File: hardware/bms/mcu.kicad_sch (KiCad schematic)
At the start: 53 parts, among them SW2 SW_Push, SW3 SW_Push, U4 LM5166X, U5 TPS62172DSG, U6 ESP32-C3-MINI-1-N4, U7 SN74LXC1T14DCKR

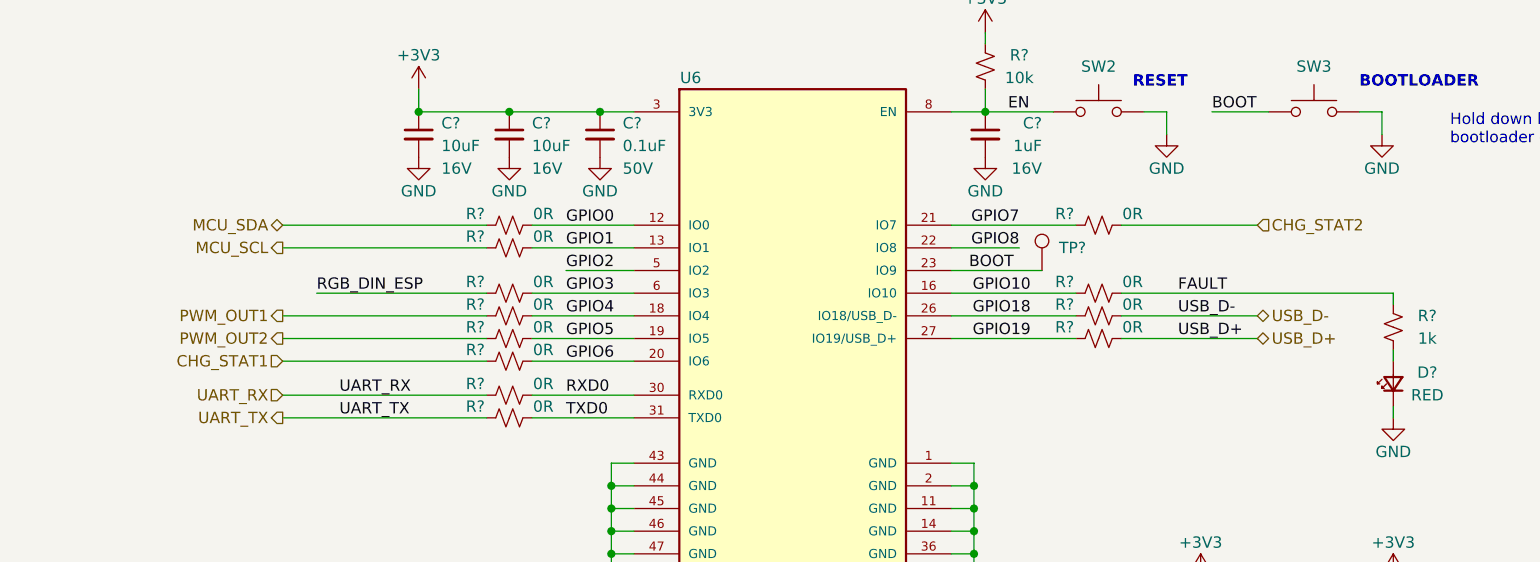
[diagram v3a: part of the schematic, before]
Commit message: Continued layout, defined board area based on mech assembly
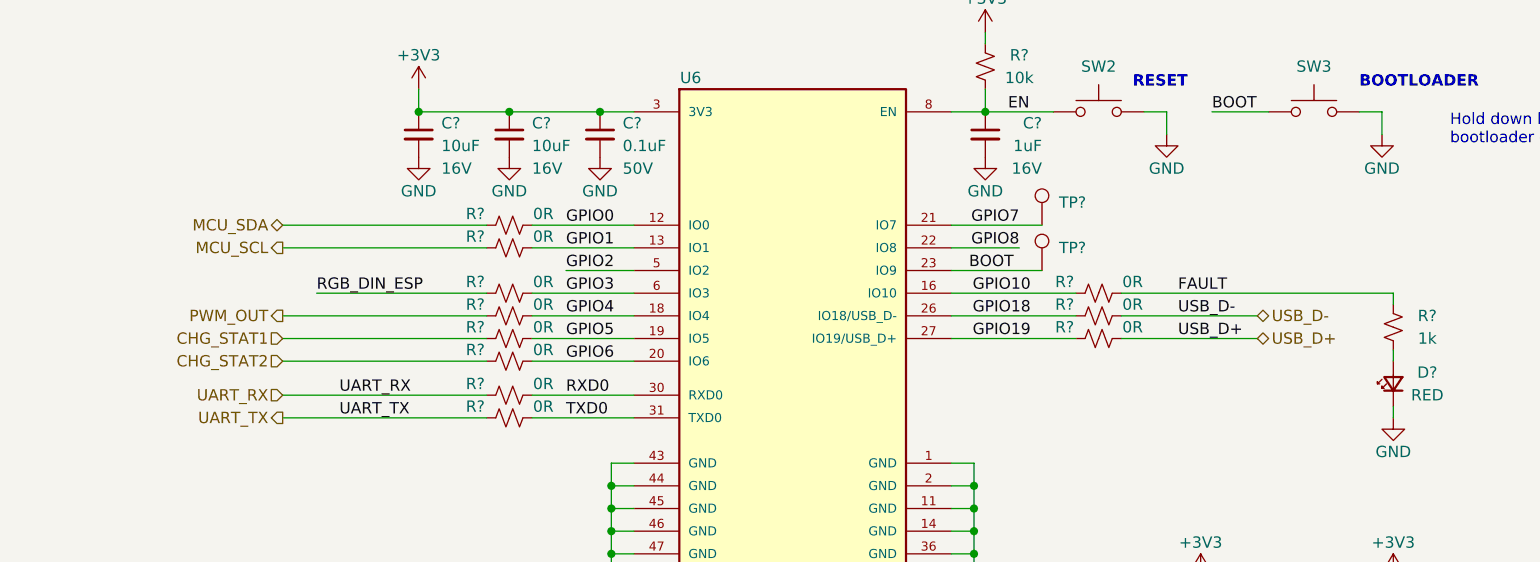
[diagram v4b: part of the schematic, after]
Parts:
- removed R?: 0R, Resistor_SMD:R_0603_1608Metric, symbol Device:R_Small_US
- added TP?: TestPoint, TestPoint:TestPoint_Pad_D1.0mm, symbol Connector:TestPoint
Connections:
- net CHG_STAT1: now also R?.1; no longer R?.1
- net CHG_STAT2: now also R?.1; no longer R?.2
- net GPIO5: now also R?.2
- net GPIO7: now also TP?.1; no longer R?.1
- net PWM_OUT1 renamed PWM_OUT
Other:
- moved on the sheet: R?
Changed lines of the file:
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@@
     (stroke (width 0) (type default))
   )
-  (wire (pts (xy 157.48 97.79) (xy 171.45 97.79))
+  (wire (pts (xy 157.48 97.79) (xy 167.64 97.79))
     (stroke (width 0) (type default))
   )
@@
     (stroke (width 0) (type default))
   )
+  (wire (pts (xy 82.55 110.49) (xy 105.41 110.49))
+    (stroke (width 0) (type default))
+  )
   (wire (pts (xy 160.02 144.78) (xy 160.02 142.24))
     (stroke (width 0) (type default))
@@
     (stroke (width 0) (type default))
   )
-  (wire (pts (xy 82.55 110.49) (xy 105.41 110.49))
-    (stroke (width 0) (type default))
-  )
   (wire (pts (xy 135.89 39.37) (xy 135.89 41.91))
     (stroke (width 0) (type default))
@@
   )
   (wire (pts (xy 91.44 172.72) (xy 99.06 172.72))
-    (stroke (width 0) (type default))
-  )
-  (wire (pts (xy 176.53 97.79) (xy 191.77 97.79))
     (stroke (width 0) (type default))
   )
@@
     (effects (font (size 1.27 1.27)) (justify left))
   )
-  (hierarchical_label "CHG_STAT2" (shape input) (at 191.77 97.79 0) (fields_autoplaced)
-    (effects (font (size 1.27 1.27)) (justify left))
-  )
-  (hierarchical_label "PWM_OUT1" (shape output) (at 82.55 107.95 180) (fields_autoplaced)
+  (hierarchical_label "CHG_STAT2" (shape input) (at 82.55 113.03 180) (fields_autoplaced)
+    (effects (font (size 1.27 1.27)) (justify right))
+  )
+  (hierarchical_label "PWM_OUT" (shape output) (at 82.55 107.95 180) (fields_autoplaced)
     (effects (font (size 1.27 1.27)) (justify right))
   )
@@
     (effects (font (size 1.27 1.27)) (justify right))
   )
-  (hierarchical_label "PWM_OUT2" (shape output) (at 82.55 110.49 180) (fields_autoplaced)
-    (effects (font (size 1.27 1.27)) (justify right))
-  )
-  (hierarchical_label "CHG_STAT1" (shape input) (at 82.55 113.03 180) (fields_autoplaced)
+  (hierarchical_label "CHG_STAT1" (shape input) (at 82.55 110.49 180) (fields_autoplaced)
     (effects (font (size 1.27 1.27)) (justify right))
   )
@@
     )
   )
-  (symbol (lib_id "Device:R_Small_US") (at 173.99 97.79 90) (unit 1)
-    (in_bom yes) (on_board yes) (dnp no)
-    (property "Reference" "R?" (at 170.18 96.52 90)
-      (effects (font (size 1.27 1.27)))
-    )
-    (property "Value" "0R" (at 177.8 96.52 90)
-      (effects (font (size 1.27 1.27)))
-    )
-    (property "Footprint" "Resistor_SMD:R_0603_1608Metric" (at 173.99 97.79 0)
-      (effects (font (size 1.27 1.27)) hide)
-    )
-    (property "Datasheet" "~" (at 173.99 97.79 0)
-      (effects (font (size 1.27 1.27)) hide)
-    )
-    (property "MFG" "Panasonic Electronic Components" (at 173.99 97.79 90)
-      (effects (font (size 1.27 1.27)) hide)
-    )
-    (property "MFG PN" "ERJ-3GEY0R00V" (at 173.99 97.79 90)
+  (symbol (lib_id "Device:R_Small_US") (at 107.95 110.49 90) (unit 1)
+    (in_bom yes) (on_board yes) (dnp no)
+    (property "Reference" "R?" (at 104.14 109.22 90)
+      (effects (font (size 1.27 1.27)))
+    )
+    (property "Value" "0R" (at 111.76 109.22 90)
+      (effects (font (size 1.27 1.27)))
+    )
+    (property "Footprint" "Resistor_SMD:R_0603_1608Metric" (at 107.95 110.49 0)
+      (effects (font (size 1.27 1.27)) hide)
+    )
+    (property "Datasheet" "~" (at 107.95 110.49 0)
+      (effects (font (size 1.27 1.27)) hide)
+    )
+    (property "MFG" "Panasonic Electronic Components" (at 107.95 110.49 90)
+      (effects (font (size 1.27 1.27)) hide)
+    )
+    (property "MFG PN" "ERJ-3GEY0R00V" (at 107.95 110.49 90)
       (effects (font (size 1.27 1.27)) hide)
     )
@@
         (path "/a4805e9d-b940-444e-a7cb-db4f4c53ed46/00000000-0000-0000-0000-00006658c265"
           (reference "#PWR038") (unit 1)
+        )
+      )
+    )
+  )
+  (symbol (lib_id "Connector:TestPoint") (at 167.64 97.79 0) (unit 1)
+    (in_bom yes) (on_board yes) (dnp no)
+    (property "Reference" "TP?" (at 169.545 95.25 0)
+      (effects (font (size 1.27 1.27)) (justify left))
+    )
+    (property "Value" "TestPoint" (at 169.1132 97.1042 0)
+      (effects (font (size 1.27 1.27)) (justify left) hide)
+    )
+    (property "Footprint" "TestPoint:TestPoint_Pad_D1.0mm" (at 172.72 97.79 0)
+      (effects (font (size 1.27 1.27)) hide)
+    )
+    (property "Datasheet" "~" (at 172.72 97.79 0)
+      (effects (font (size 1.27 1.27)) hide)
+    )
+    (pin "1")
+    (instances
+      (project "bms"
+        (path "/a4805e9d-b940-444e-a7cb-db4f4c53ed46/00000000-0000-0000-0000-00006523a805"
+          (reference "TP?") (unit 1)
+        )
+        (path "/a4805e9d-b940-444e-a7cb-db4f4c53ed46/00000000-0000-0000-0000-00006658c265"
+          (reference "TP65") (unit 1)
         )
       )
@@
         )
       )
-    )
-  )
-  (symbol (lib_id "Device:R_Small_US") (at 107.95 110.49 90) (unit 1)
-    (in_bom yes) (on_board yes) (dnp no)
-    (property "Reference" "R?" (at 104.14 109.22 90)
-      (effects (font (size 1.27 1.27)))
-    )
-    (property "Value" "0R" (at 111.76 109.22 90)
-      (effects (font (size 1.27 1.27)))
-    )
-    (property "Footprint" "Resistor_SMD:R_0603_1608Metric" (at 107.95 110.49 0)
-      (effects (font (size 1.27 1.27)) hide)
-    )
-    (property "Datasheet" "~" (at 107.95 110.49 0)
-      (effects (font (size 1.27 1.27)) hide)
-    )
-    (property "MFG" "Panasonic Electronic Components" (at 107.95 110.49 90)
-      (effects (font (size 1.27 1.27)) hide)
-    )
-    (property "MFG PN" "ERJ-3GEY0R00V" (at 107.95 110.49 90)
-      (effects (font (size 1.27 1.27)) hide)
-    )
-    (pin "1")
-    (pin "2")
-    (instances
-      (project "bms"
-        (path "/a4805e9d-b940-444e-a7cb-db4f4c53ed46/00000000-0000-0000-0000-00006523a805"
-          (reference "R?") (unit 1)
-        )
-        (path "/a4805e9d-b940-444e-a7cb-db4f4c53ed46/00000000-0000-0000-0000-00006658c265"
-          (reference "R72") (unit 1)
-        )
-      )

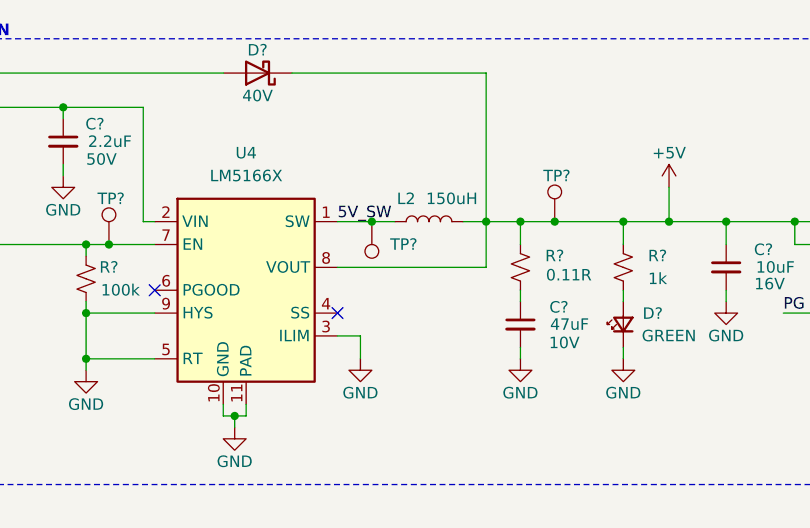
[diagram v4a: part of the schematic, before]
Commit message: Updated test points to 0.5mm to save space, continued layout
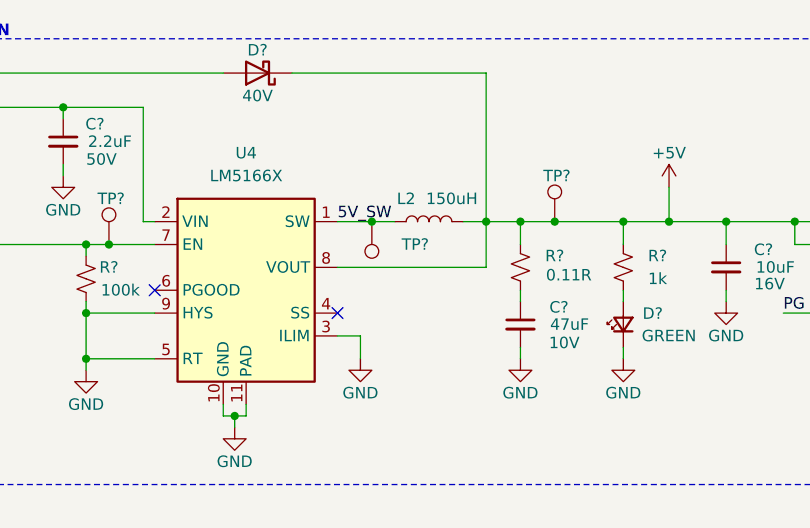
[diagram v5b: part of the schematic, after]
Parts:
- TP? (x9): footprint TestPoint:TestPoint_Pad_D1.0mm -> bms:TestPoint_Pad_D0.5mm; now left out of the parts list
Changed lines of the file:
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@@
   )
   (symbol (lib_id "Connector:TestPoint") (at 99.06 172.72 180) (unit 1)
-    (in_bom yes) (on_board yes) (dnp no)
+    (in_bom no) (on_board yes) (dnp no)
     (property "Reference" "TP?" (at 101.3409 178.1614 0)
       (effects (font (size 1.27 1.27)) (justify left))
@@
       (effects (font (size 1.27 1.27)) (justify left) hide)
     )
-    (property "Footprint" "TestPoint:TestPoint_Pad_D1.0mm" (at 93.98 172.72 0)
+    (property "Footprint" "bms:TestPoint_Pad_D0.5mm" (at 93.98 172.72 0)
       (effects (font (size 1.27 1.27)) hide)
     )
@@
   )
   (symbol (lib_id "Connector:TestPoint") (at 128.27 39.37 0) (unit 1)
-    (in_bom yes) (on_board yes) (dnp no)
+    (in_bom no) (on_board yes) (dnp no)
     (property "Reference" "TP?" (at 127 34.29 0)
       (effects (font (size 1.27 1.27)) (justify left))
@@
       (effects (font (size 1.27 1.27)) (justify left) hide)
     )
-    (property "Footprint" "TestPoint:TestPoint_Pad_D1.0mm" (at 133.35 39.37 0)
+    (property "Footprint" "bms:TestPoint_Pad_D0.5mm" (at 133.35 39.37 0)
       (effects (font (size 1.27 1.27)) hide)
     )
@@
   )
   (symbol (lib_id "Connector:TestPoint") (at 73.66 172.72 180) (unit 1)
-    (in_bom yes) (on_board yes) (dnp no)
+    (in_bom no) (on_board yes) (dnp no)
     (property "Reference" "TP?" (at 75.7005 178.1614 0)
       (effects (font (size 1.27 1.27)) (justify left))
@@
       (effects (font (size 1.27 1.27)) (justify left) hide)
     )
-    (property "Footprint" "TestPoint:TestPoint_Pad_D1.0mm" (at 68.58 172.72 0)
+    (property "Footprint" "bms:TestPoint_Pad_D0.5mm" (at 68.58 172.72 0)
       (effects (font (size 1.27 1.27)) hide)
     )
@@
   )
   (symbol (lib_id "Connector:TestPoint") (at 167.64 97.79 0) (unit 1)
-    (in_bom yes) (on_board yes) (dnp no)
+    (in_bom no) (on_board yes) (dnp no)
     (property "Reference" "TP?" (at 169.545 95.25 0)
       (effects (font (size 1.27 1.27)) (justify left))
@@
       (effects (font (size 1.27 1.27)) (justify left) hide)
     )
-    (property "Footprint" "TestPoint:TestPoint_Pad_D1.0mm" (at 172.72 97.79 0)
+    (property "Footprint" "bms:TestPoint_Pad_D0.5mm" (at 172.72 97.79 0)
       (effects (font (size 1.27 1.27)) hide)
     )
@@
   )
   (symbol (lib_id "Connector:TestPoint") (at 186.69 39.37 0) (unit 1)
-    (in_bom yes) (on_board yes) (dnp no)
+    (in_bom no) (on_board yes) (dnp no)
     (property "Reference" "TP?" (at 185.42 34.29 0)
       (effects (font (size 1.27 1.27)) (justify left))
@@
       (effects (font (size 1.27 1.27)) (justify left) hide)
     )
-    (property "Footprint" "TestPoint:TestPoint_Pad_D1.0mm" (at 191.77 39.37 0)
+    (property "Footprint" "bms:TestPoint_Pad_D0.5mm" (at 191.77 39.37 0)
       (effects (font (size 1.27 1.27)) hide)
     )
@@
   )
   (symbol (lib_id "Connector:TestPoint") (at 107.95 39.37 180) (unit 1)
-    (in_bom yes) (on_board yes) (dnp no)
-    (property "Reference" "TP?" (at 113.03 41.91 0)
+    (in_bom no) (on_board yes) (dnp no)
+    (property "Reference" "TP?" (at 114.3 41.91 0)
       (effects (font (size 1.27 1.27)) (justify left))
     )
@@
       (effects (font (size 1.27 1.27)) (justify left) hide)
     )
-    (property "Footprint" "TestPoint:TestPoint_Pad_D1.0mm" (at 102.87 39.37 0)
+    (property "Footprint" "bms:TestPoint_Pad_D0.5mm" (at 102.87 39.37 0)
       (effects (font (size 1.27 1.27)) hide)
     )
@@
   )
   (symbol (lib_id "Connector:TestPoint") (at 167.64 102.87 0) (unit 1)
-    (in_bom yes) (on_board yes) (dnp no)
+    (in_bom no) (on_board yes) (dnp no)
     (property "Reference" "TP?" (at 169.545 100.33 0)
       (effects (font (size 1.27 1.27)) (justify left))
@@
       (effects (font (size 1.27 1.27)) (justify left) hide)
     )
-    (property "Footprint" "TestPoint:TestPoint_Pad_D1.0mm" (at 172.72 102.87 0)
+    (property "Footprint" "bms:TestPoint_Pad_D0.5mm" (at 172.72 102.87 0)
       (effects (font (size 1.27 1.27)) hide)
     )
@@
   )
   (symbol (lib_id "Connector:TestPoint") (at 209.55 39.37 0) (unit 1)
-    (in_bom yes) (on_board yes) (dnp no)
+    (in_bom no) (on_board yes) (dnp no)
     (property "Reference" "TP?" (at 208.28 34.29 0)
       (effects (font (size 1.27 1.27)) (justify left))
@@
       (effects (font (size 1.27 1.27)) (justify left) hide)
     )
-    (property "Footprint" "TestPoint:TestPoint_Pad_D1.0mm" (at 214.63 39.37 0)
+    (property "Footprint" "bms:TestPoint_Pad_D0.5mm" (at 214.63 39.37 0)
       (effects (font (size 1.27 1.27)) hide)
     )
@@
   )
   (symbol (lib_id "Connector:TestPoint") (at 78.74 41.91 0) (unit 1)
-    (in_bom yes) (on_board yes) (dnp no)
+    (in_bom no) (on_board yes) (dnp no)
     (property "Reference" "TP?" (at 77.47 36.83 0)
       (effects (font (size 1.27 1.27)) (justify left))
@@
       (effects (font (size 1.27 1.27)) (justify left) hide)
     )
-    (property "Footprint" "TestPoint:TestPoint_Pad_D1.0mm" (at 83.82 41.91 0)
-      (effects (font (size 1.27 1.27)) hide)
-    )
+    (property "Footprint" "bms:TestPoint_Pad_D0.5mm" (at 83.82 41.91 0)
+      (effects (font (size 1.27 1.27)) hide)
+    )
